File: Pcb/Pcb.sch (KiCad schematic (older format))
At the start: 129 parts, among them J1 TRRS, Q1 2N7002, SW1 SW_Push, SW10 SW_Push, SW11 SW_Push, SW12 SW_Push, SW13 SW_Push, SW14 SW_Push, SW15 SW_Push, SW16 SW_Push, SW17 SW_Push, SW18 SW_Push, SW19 SW_Push, SW2 SW2, SW20 SW_Push, SW21 SW_Push, SW22 SW_Push, SW23 SW_Push, SW24 SW_Push, SW25 SW_Push, SW26 SW_Push, SW27 SW_Push, SW28 SW_Push, SW29 SW_Push, SW3 SW_Push, SW4 SW_Push, SW5 SW_Push, SW6 SW_Push, SW7 SW_Push, SW8 SW_Push, SW9 SW_Push, U1 ProMicro

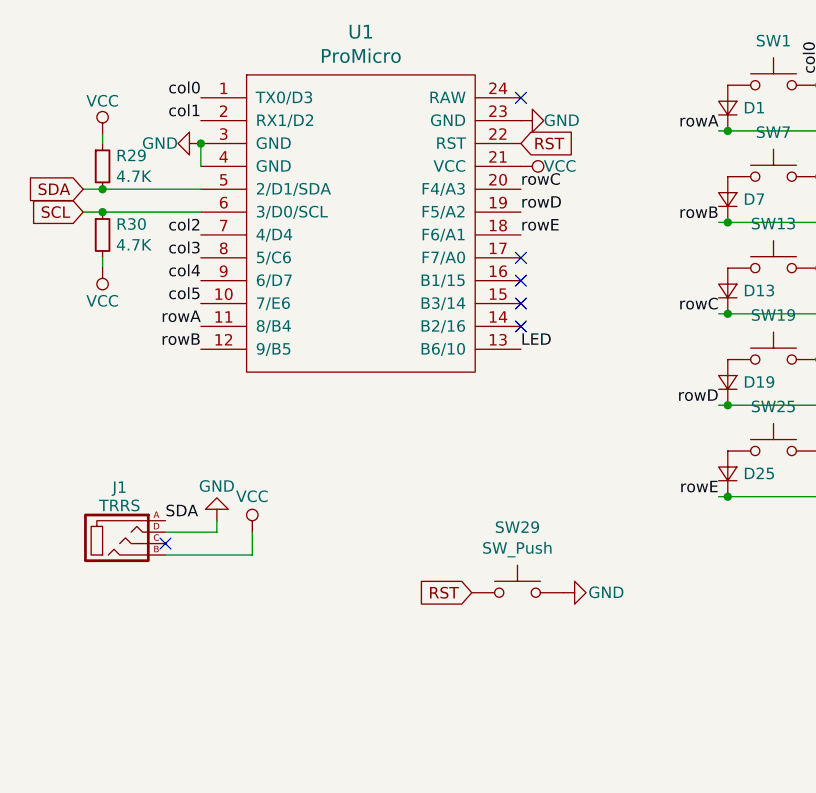
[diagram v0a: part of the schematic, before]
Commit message: Add jumpers for TRRS jack
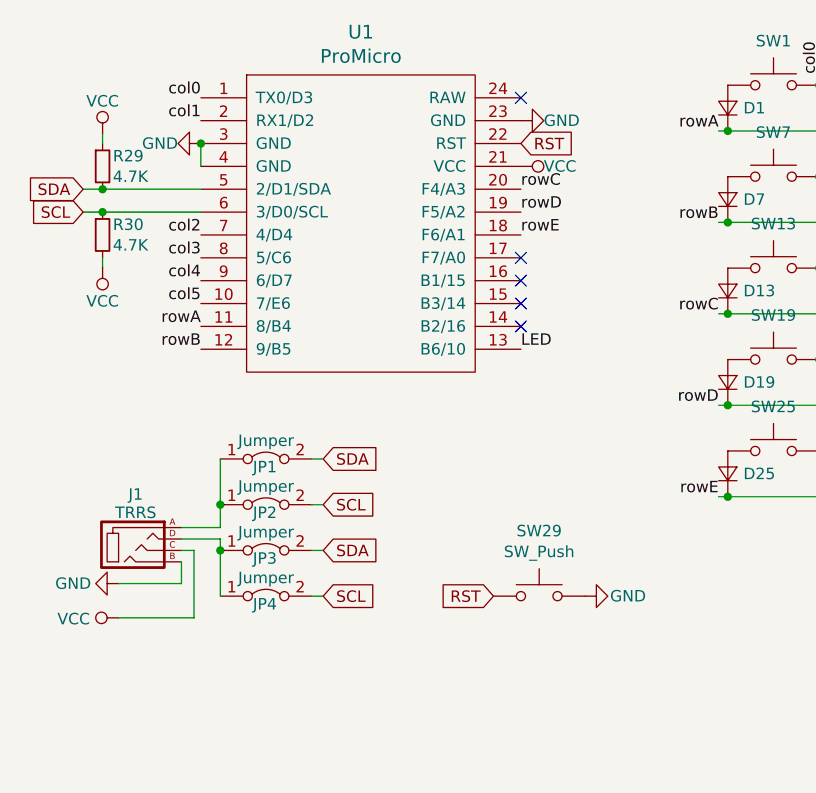
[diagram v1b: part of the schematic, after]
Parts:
- added JP1, JP2, JP3, JP4: Jumper, symbol Jumper:Jumper_2_Bridged
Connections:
- net GND: now also J1.B; no longer J1.D
- net SCL: now also JP2.2 (B), JP4.2 (B)
- net SDA: now also JP1.2 (B), JP3.2 (B); no longer J1.A
- net VCC: now also J1.C; no longer J1.B
- new net: J1.A, JP1.1 (A), JP2.1 (A)
- new net: J1.D, JP3.1 (A), JP4.1 (A)
- no-connect marks 6 -> 5
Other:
- moved on the sheet: J1, SW29
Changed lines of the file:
@@
 L Switch:SW_Push SW29
 U 1 1 5DBF73FF
-P 2625 3110
-F 0 "SW29" H 2625 3395 50  0000 C CNN
-F 1 "SW_Push" H 2625 3304 50  0000 C CNN
-F 2 "Used_Footprints:Switch_Reset_THT" H 2625 3310 50  0001 C CNN
-F 3 "~" H 2625 3310 50  0001 C CNN
-	1    2625 3110
+P 2720 3125
+F 0 "SW29" H 2720 3410 50  0000 C CNN
+F 1 "SW_Push" H 2720 3319 50  0000 C CNN
+F 2 "Used_Footprints:Switch_Reset_THT" H 2720 3325 50  0001 C CNN
+F 3 "~" H 2720 3325 50  0001 C CNN
+	1    2720 3125
 	1    0    0    -1
 $EndComp
@@
 L power:GND #PWR01
 U 1 1 5DBF973E
-P 2825 3110
-F 0 "#PWR01" H 2825 2860 50  0001 C CNN
-F 1 "GND" V 2825 3000 50  0000 R CNN
-F 2 "" H 2825 3110 50  0001 C CNN
-F 3 "" H 2825 3110 50  0001 C CNN
-	1    2825 3110
+P 2920 3125
+F 0 "#PWR01" H 2920 2875 50  0001 C CNN
+F 1 "GND" V 2920 3015 50  0000 R CNN
+F 2 "" H 2920 3125 50  0001 C CNN
+F 3 "" H 2920 3125 50  0001 C CNN
+	1    2920 3125
 	0    -1   -1   0
 $EndComp
@@
 L kbd:MJ-4PP-9 J1
 U 1 1 5DBFACF7
-P 885 2870
-F 0 "J1" H 885 3090 50  0000 C CNN
-F 1 "TRRS" H 885 3010 50  0000 C CNN
-F 2 "Used_Footprints:TRSS_DUAL_THT" H 1160 3045 50  0001 C CNN
-F 3 "~" H 1160 3045 50  0001 C CNN
-	1    885  2870
-	1    0    0    -1
-$EndComp
-Text GLabel 2425 3110 0    50   Input ~ 0
+P 955 2900
+F 0 "J1" H 955 3120 50  0000 C CNN
+F 1 "TRRS" H 955 3040 50  0000 C CNN
+F 2 "Used_Footprints:TRSS_DUAL_THT" H 1230 3075 50  0001 C CNN
+F 3 "~" H 1230 3075 50  0001 C CNN
+	1    955  2900
+	1    0    0    -1
+$EndComp
+Text GLabel 2520 3125 0    50   Input ~ 0
 RST
 Text GLabel 2640 1145 2    50   Input ~ 0
@@
 NoConn ~ 2640 1845
 NoConn ~ 2640 1745
-Text Label 1085 2795 0    50   ~ 0
-SDA
-$Comp
-L power:GND #PWR0101
-U 1 1 5E5516DF
-P 1310 2795
-F 0 "#PWR0101" H 1310 2545 50  0001 C CNN
-F 1 "GND" H 1310 2645 50  0000 C CNN
-F 2 "" H 1310 2795 50  0001 C CNN
-F 3 "" H 1310 2795 50  0001 C CNN
-	1    1310 2795
-	-1   0    0    1
-$EndComp
-Wire Wire Line
-	1085 2845 1310 2845
-Wire Wire Line
-	1310 2845 1310 2795
-$Comp
-L power:VCC #PWR0102
-U 1 1 5E557C13
-P 1465 2845
-F 0 "#PWR0102" H 1465 2695 50  0001 C CNN
-F 1 "VCC" H 1465 3000 50  0000 C CNN
-F 2 "" H 1465 2845 50  0001 C CNN
-F 3 "" H 1465 2845 50  0001 C CNN
-	1    1465 2845
-	1    0    0    -1
-$EndComp
-Wire Wire Line
-	1465 2845 1465 2945
-Wire Wire Line
-	1465 2945 1085 2945
-NoConn ~ 1085 2895
 Connection ~ 1240 1145
 $Comp
@@
 U 1 1 5E5A5774
 P 810 1245
-F 0 "R29" H 869 1291 50  0000 L CNN
-F 1 "4.7K" H 869 1200 50  0000 L CNN
+F 0 "R29" H 855 1290 50  0000 L CNN
+F 1 "4.7K" H 855 1200 50  0000 L CNN
 F 2 "" H 810 1245 50  0001 C CNN
 F 3 "~" H 810 1245 50  0001 C CNN
@@
 U 1 1 5E5A67AE
 P 810 1545
-F 0 "R30" H 869 1591 50  0000 L CNN
-F 1 "4.7K" H 869 1500 50  0000 L CNN
+F 0 "R30" H 855 1590 50  0000 L CNN
+F 1 "4.7K" H 855 1500 50  0000 L CNN
 F 2 "" H 810 1545 50  0001 C CNN
 F 3 "~" H 810 1545 50  0001 C CNN
@@
 Wire Wire Line
 	810  1105 810  1145
+$Comp
+L Jumper:Jumper_2_Bridged JP1
+U 1 1 5E612479
+P 1525 2525
+F 0 "JP1" H 1520 2490 50  0000 C CNN
+F 1 "Jumper" H 1525 2605 50  0000 C CNN
+F 2 "" H 1525 2525 50  0001 C CNN
+F 3 "~" H 1525 2525 50  0001 C CNN
+	1    1525 2525
+	1    0    0    -1
+$EndComp
+$Comp
+L Jumper:Jumper_2_Bridged JP2
+U 1 1 5E61A832
+P 1525 2725
+F 0 "JP2" H 1520 2690 50  0000 C CNN
+F 1 "Jumper" H 1525 2805 50  0000 C CNN
+F 2 "" H 1525 2725 50  0001 C CNN
+F 3 "~" H 1525 2725 50  0001 C CNN
+	1    1525 2725
+	1    0    0    -1
+$EndComp
+$Comp
+L Jumper:Jumper_2_Bridged JP3
+U 1 1 5E622F25
+P 1525 2925
+F 0 "JP3" H 1520 2890 50  0000 C CNN
+F 1 "Jumper" H 1525 3005 50  0000 C CNN
+F 2 "" H 1525 2925 50  0001 C CNN
+F 3 "~" H 1525 2925 50  0001 C CNN
+	1    1525 2925
+	1    0    0    -1
+$EndComp
+$Comp
+L Jumper:Jumper_2_Bridged JP4
+U 1 1 5E622F2B
+P 1525 3125
+F 0 "JP4" H 1520 3090 50  0000 C CNN
+F 1 "Jumper" H 1525 3205 50  0000 C CNN
+F 2 "" H 1525 3125 50  0001 C CNN
+F 3 "~" H 1525 3125 50  0001 C CNN
+	1    1525 3125
+	1    0    0    -1
+$EndComp
+Wire Wire Line
+	1325 2525 1325 2725
+Wire Wire Line
+	1325 2825 1155 2825
+Connection ~ 1325 2725
+Wire Wire Line
+	1325 2725 1325 2825
+Wire Wire Line
+	1325 3125 1325 2925
+Wire Wire Line
+	1325 2875 1155 2875
+Connection ~ 1325 2925
+Wire Wire Line
+	1325 2925 1325 2875
+Text GLabel 1775 2525 2    50   Input ~ 0
+SDA
+Wire Wire Line
+	1775 2525 1725 2525
+Text GLabel 1775 2725 2    50   Input ~ 0
+SCL
+Wire Wire Line
+	1775 2725 1725 2725
+Text GLabel 1775 2925 2    50   Input ~ 0
+SDA
+Wire Wire Line
+	1775 2925 1725 2925
+Text GLabel 1775 3125 2    50   Input ~ 0
+SCL
+Wire Wire Line
+	1775 3125 1725 3125
+$Comp
+L power:GND #PWR?
+U 1 1 5E653D30
+P 880 3070
+F 0 "#PWR?" H 880 2820 50  0001 C CNN
+F 1 "GND" V 880 2950 50  0000 R CNN
+F 2 "" H 880 3070 50  0001 C CNN
+F 3 "" H 880 3070 50  0001 C CNN
+	1    880  3070
+	0    1    1    0
+$EndComp
+Wire Wire Line
+	880  3070 1155 3070
+Wire Wire Line
+	1155 3070 1155 2975
+$Comp
+L power:VCC #PWR?
+U 1 1 5E65ED2C
+P 880 3220
+F 0 "#PWR?" H 880 3070 50  0001 C CNN
+F 1 "VCC" V 875 3345 50  0000 L CNN
+F 2 "" H 880 3220 50  0001 C CNN
+F 3 "" H 880 3220 50  0001 C CNN
+	1    880  3220
+	0    -1   -1   0
+$EndComp
+Wire Wire Line
+	1210 3220 1210 2925
+Wire Wire Line
+	1210 2925 1155 2925
+Wire Wire Line
+	880  3220 1210 3220
 $EndSCHEMATC

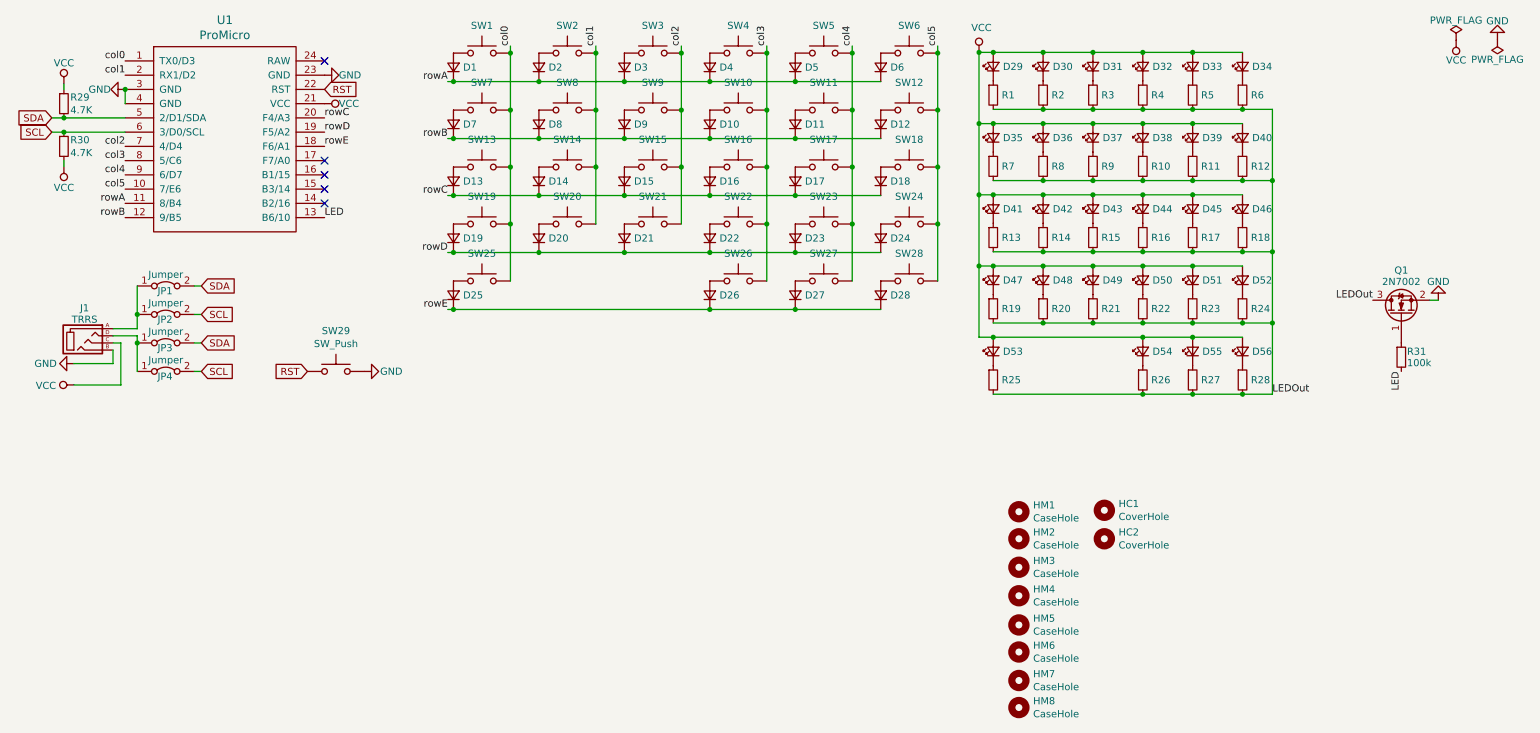
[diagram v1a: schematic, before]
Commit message: Add value for resistors
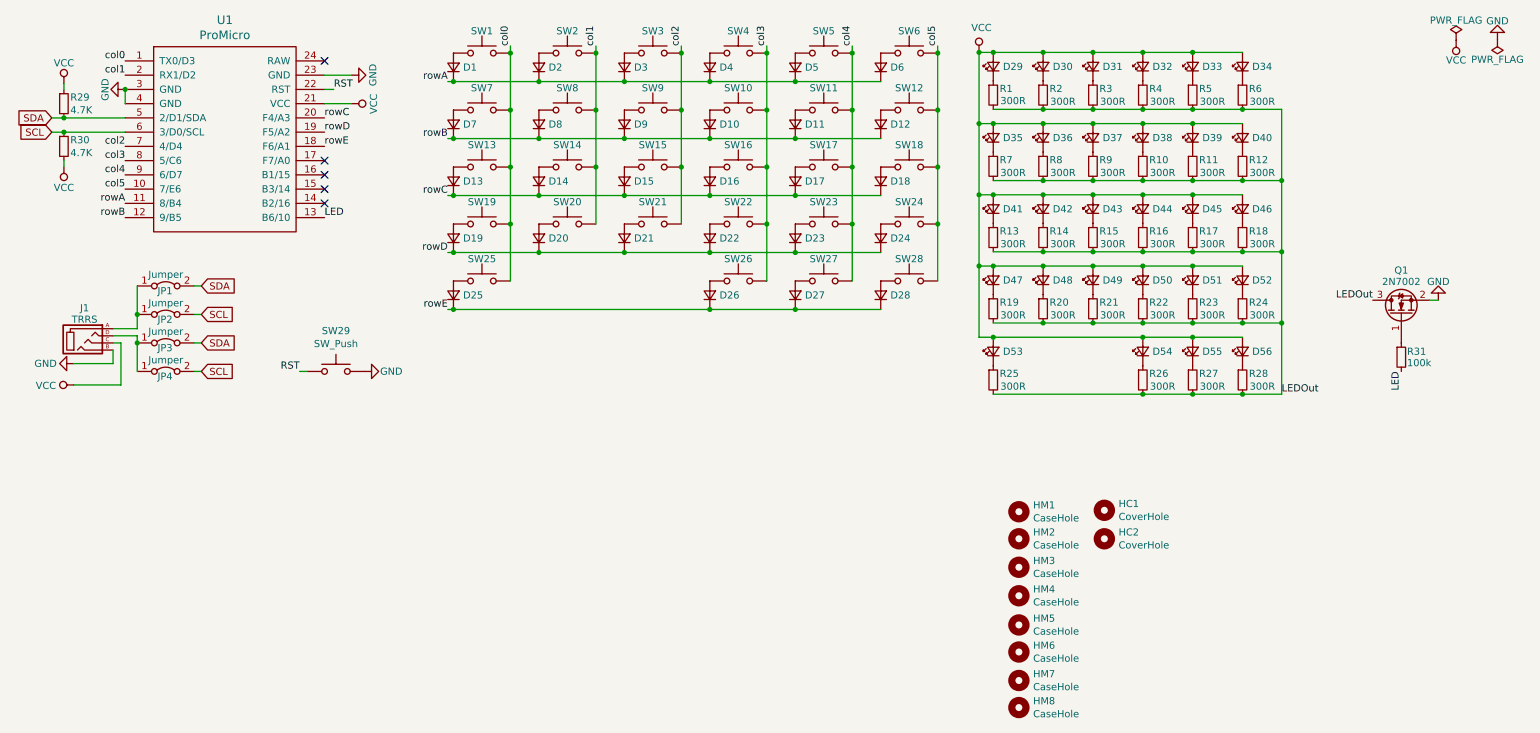
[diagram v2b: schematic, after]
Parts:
- R1, R10, R11, R12, R13, R14, R15, R16, R17, R18, R19, R2, R20, R21, R22, R23, R24, R25, R26, R27, R28, R3, R4, R5, R6, R7, R8, R9: value R_Small -> 300R

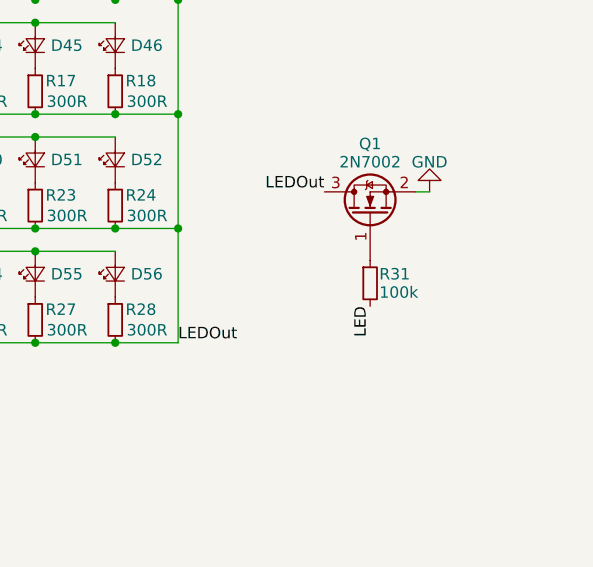
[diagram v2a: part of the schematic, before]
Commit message: Add value for diodes
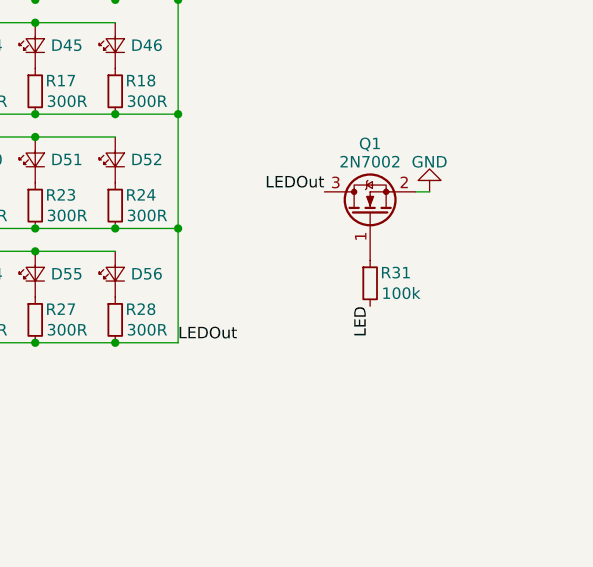
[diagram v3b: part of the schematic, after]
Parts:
- D1, D10, D11, D12, D13, D14, D15, D16, D17, D18, D19, D2, D20, D21, D22, D23, D24, D25, D26, D27, D28, D3, D4, D5, D6, D7, D8, D9: value D_Small -> 1N4148
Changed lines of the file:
@@
 P 3545 990
 F 0 "D1" V 3545 922 50  0000 R CNN
-F 1 "D_Small" V 3500 922 50  0001 R CNN
+F 1 "1N4148" V 3500 922 50  0001 R CNN
 F 2 "Used_Footprints:Diode_Hybrid_SOD-123" V 3545 990 50  0001 C CNN
 F 3 "~" V 3545 990 50  0001 C CNN
@@
 P 4145 990
 F 0 "D2" V 4145 922 50  0000 R CNN
-F 1 "D_Small" V 4100 922 50  0001 R CNN
+F 1 "1N4148" V 4100 922 50  0001 R CNN
 F 2 "Used_Footprints:Diode_Hybrid_SOD-123" V 4145 990 50  0001 C CNN
 F 3 "~" V 4145 990 50  0001 C CNN
@@
 P 4745 990
 F 0 "D3" V 4745 922 50  0000 R CNN
-F 1 "D_Small" V 4700 922 50  0001 R CNN
+F 1 "1N4148" V 4700 922 50  0001 R CNN
 F 2 "Used_Footprints:Diode_Hybrid_SOD-123" V 4745 990 50  0001 C CNN
 F 3 "~" V 4745 990 50  0001 C CNN
@@
 P 5345 990
 F 0 "D4" V 5345 922 50  0000 R CNN
-F 1 "D_Small" V 5300 922 50  0001 R CNN
+F 1 "1N4148" V 5300 922 50  0001 R CNN
 F 2 "Used_Footprints:Diode_Hybrid_SOD-123" V 5345 990 50  0001 C CNN
 F 3 "~" V 5345 990 50  0001 C CNN
@@
 P 5945 990
 F 0 "D5" V 5945 922 50  0000 R CNN
-F 1 "D_Small" V 5900 922 50  0001 R CNN
+F 1 "1N4148" V 5900 922 50  0001 R CNN
 F 2 "Used_Footprints:Diode_Hybrid_SOD-123" V 5945 990 50  0001 C CNN
 F 3 "~" V 5945 990 50  0001 C CNN
@@
 P 6545 990
 F 0 "D6" V 6545 922 50  0000 R CNN
-F 1 "D_Small" V 6500 922 50  0001 R CNN
+F 1 "1N4148" V 6500 922 50  0001 R CNN
 F 2 "Used_Footprints:Diode_Hybrid_SOD-123" V 6545 990 50  0001 C CNN
 F 3 "~" V 6545 990 50  0001 C CNN
@@
 P 3545 1390
 F 0 "D7" V 3545 1322 50  0000 R CNN
-F 1 "D_Small" V 3500 1322 50  0001 R CNN
+F 1 "1N4148" V 3500 1322 50  0001 R CNN
 F 2 "Used_Footprints:Diode_Hybrid_SOD-123" V 3545 1390 50  0001 C CNN
 F 3 "~" V 3545 1390 50  0001 C CNN
@@
 P 4145 1390
 F 0 "D8" V 4145 1322 50  0000 R CNN
-F 1 "D_Small" V 4100 1322 50  0001 R CNN
+F 1 "1N4148" V 4100 1322 50  0001 R CNN
 F 2 "Used_Footprints:Diode_Hybrid_SOD-123" V 4145 1390 50  0001 C CNN
 F 3 "~" V 4145 1390 50  0001 C CNN
@@
 P 4745 1390
 F 0 "D9" V 4745 1322 50  0000 R CNN
-F 1 "D_Small" V 4700 1322 50  0001 R CNN
+F 1 "1N4148" V 4700 1322 50  0001 R CNN
 F 2 "Used_Footprints:Diode_Hybrid_SOD-123" V 4745 1390 50  0001 C CNN
 F 3 "~" V 4745 1390 50  0001 C CNN
@@
 P 5345 1390
 F 0 "D10" V 5345 1322 50  0000 R CNN
-F 1 "D_Small" V 5300 1322 50  0001 R CNN
+F 1 "1N4148" V 5300 1322 50  0001 R CNN
 F 2 "Used_Footprints:Diode_Hybrid_SOD-123" V 5345 1390 50  0001 C CNN
 F 3 "~" V 5345 1390 50  0001 C CNN
@@
 P 5945 1390
 F 0 "D11" V 5945 1322 50  0000 R CNN
-F 1 "D_Small" V 5900 1322 50  0001 R CNN
+F 1 "1N4148" V 5900 1322 50  0001 R CNN
 F 2 "Used_Footprints:Diode_Hybrid_SOD-123" V 5945 1390 50  0001 C CNN
 F 3 "~" V 5945 1390 50  0001 C CNN
@@
 P 6545 1390
 F 0 "D12" V 6545 1322 50  0000 R CNN
-F 1 "D_Small" V 6500 1322 50  0001 R CNN
+F 1 "1N4148" V 6500 1322 50  0001 R CNN
 F 2 "Used_Footprints:Diode_Hybrid_SOD-123" V 6545 1390 50  0001 C CNN
 F 3 "~" V 6545 1390 50  0001 C CNN
@@
 P 3545 1790
 F 0 "D13" V 3545 1722 50  0000 R CNN
-F 1 "D_Small" V 3500 1722 50  0001 R CNN
+F 1 "1N4148" V 3500 1722 50  0001 R CNN
 F 2 "Used_Footprints:Diode_Hybrid_SOD-123" V 3545 1790 50  0001 C CNN
 F 3 "~" V 3545 1790 50  0001 C CNN
@@
 P 4145 1790
 F 0 "D14" V 4145 1722 50  0000 R CNN
-F 1 "D_Small" V 4100 1722 50  0001 R CNN
+F 1 "1N4148" V 4100 1722 50  0001 R CNN
 F 2 "Used_Footprints:Diode_Hybrid_SOD-123" V 4145 1790 50  0001 C CNN
 F 3 "~" V 4145 1790 50  0001 C CNN
@@
 P 4745 1790
 F 0 "D15" V 4745 1722 50  0000 R CNN
-F 1 "D_Small" V 4700 1722 50  0001 R CNN
+F 1 "1N4148" V 4700 1722 50  0001 R CNN
 F 2 "Used_Footprints:Diode_Hybrid_SOD-123" V 4745 1790 50  0001 C CNN
 F 3 "~" V 4745 1790 50  0001 C CNN
@@
 P 5345 1790
 F 0 "D16" V 5345 1722 50  0000 R CNN
-F 1 "D_Small" V 5300 1722 50  0001 R CNN
+F 1 "1N4148" V 5300 1722 50  0001 R CNN
 F 2 "Used_Footprints:Diode_Hybrid_SOD-123" V 5345 1790 50  0001 C CNN
 F 3 "~" V 5345 1790 50  0001 C CNN
@@
 P 5945 1790
 F 0 "D17" V 5945 1722 50  0000 R CNN
-F 1 "D_Small" V 5900 1722 50  0001 R CNN
+F 1 "1N4148" V 5900 1722 50  0001 R CNN
 F 2 "Used_Footprints:Diode_Hybrid_SOD-123" V 5945 1790 50  0001 C CNN
 F 3 "~" V 5945 1790 50  0001 C CNN
@@
 P 6545 1790
 F 0 "D18" V 6545 1722 50  0000 R CNN
-F 1 "D_Small" V 6500 1722 50  0001 R CNN
+F 1 "1N4148" V 6500 1722 50  0001 R CNN
 F 2 "Used_Footprints:Diode_Hybrid_SOD-123" V 6545 1790 50  0001 C CNN
 F 3 "~" V 6545 1790 50  0001 C CNN
@@
 P 3545 2190
 F 0 "D19" V 3545 2122 50  0000 R CNN
-F 1 "D_Small" V 3500 2122 50  0001 R CNN
+F 1 "1N4148" V 3500 2122 50  0001 R CNN
 F 2 "Used_Footprints:Diode_Hybrid_SOD-123" V 3545 2190 50  0001 C CNN
 F 3 "~" V 3545 2190 50  0001 C CNN
@@
 P 4145 2190
 F 0 "D20" V 4145 2122 50  0000 R CNN
-F 1 "D_Small" V 4100 2122 50  0001 R CNN
+F 1 "1N4148" V 4100 2122 50  0001 R CNN
 F 2 "Used_Footprints:Diode_Hybrid_SOD-123" V 4145 2190 50  0001 C CNN
 F 3 "~" V 4145 2190 50  0001 C CNN
@@
 P 4745 2190
 F 0 "D21" V 4745 2122 50  0000 R CNN
-F 1 "D_Small" V 4700 2122 50  0001 R CNN
+F 1 "1N4148" V 4700 2122 50  0001 R CNN
 F 2 "Used_Footprints:Diode_Hybrid_SOD-123" V 4745 2190 50  0001 C CNN
 F 3 "~" V 4745 2190 50  0001 C CNN
@@
 P 5345 2190
 F 0 "D22" V 5345 2122 50  0000 R CNN
-F 1 "D_Small" V 5300 2122 50  0001 R CNN
+F 1 "1N4148" V 5300 2122 50  0001 R CNN
 F 2 "Used_Footprints:Diode_Hybrid_SOD-123" V 5345 2190 50  0001 C CNN
 F 3 "~" V 5345 2190 50  0001 C CNN
@@
 P 5945 2190
 F 0 "D23" V 5945 2122 50  0000 R CNN
-F 1 "D_Small" V 5900 2122 50  0001 R CNN
+F 1 "1N4148" V 5900 2122 50  0001 R CNN
 F 2 "Used_Footprints:Diode_Hybrid_SOD-123" V 5945 2190 50  0001 C CNN
 F 3 "~" V 5945 2190 50  0001 C CNN
@@
 P 6545 2190
 F 0 "D24" V 6545 2122 50  0000 R CNN
-F 1 "D_Small" V 6500 2122 50  0001 R CNN
+F 1 "1N4148" V 6500 2122 50  0001 R CNN
 F 2 "Used_Footprints:Diode_Hybrid_SOD-123" V 6545 2190 50  0001 C CNN
 F 3 "~" V 6545 2190 50  0001 C CNN
@@
 P 3545 2590
 F 0 "D25" V 3545 2522 50  0000 R CNN
-F 1 "D_Small" V 3500 2522 50  0001 R CNN
+F 1 "1N4148" V 3500 2522 50  0001 R CNN
 F 2 "Used_Footprints:Diode_Hybrid_SOD-123" V 3545 2590 50  0001 C CNN
 F 3 "~" V 3545 2590 50  0001 C CNN
@@
 P 5345 2590
 F 0 "D26" V 5345 2522 50  0000 R CNN
-F 1 "D_Small" V 5300 2522 50  0001 R CNN
+F 1 "1N4148" V 5300 2522 50  0001 R CNN
 F 2 "Used_Footprints:Diode_Hybrid_SOD-123" V 5345 2590 50  0001 C CNN
 F 3 "~" V 5345 2590 50  0001 C CNN
@@
 P 5945 2590
 F 0 "D27" V 5945 2522 50  0000 R CNN
-F 1 "D_Small" V 5900 2522 50  0001 R CNN
+F 1 "1N4148" V 5900 2522 50  0001 R CNN
 F 2 "Used_Footprints:Diode_Hybrid_SOD-123" V 5945 2590 50  0001 C CNN
 F 3 "~" V 5945 2590 50  0001 C CNN
@@
 P 6545 2590
 F 0 "D28" V 6545 2522 50  0000 R CNN
-F 1 "D_Small" V 6500 2522 50  0001 R CNN
+F 1 "1N4148" V 6500 2522 50  0001 R CNN
 F 2 "Used_Footprints:Diode_Hybrid_SOD-123" V 6545 2590 50  0001 C CNN
 F 3 "~" V 6545 2590 50  0001 C CNN
@@
 U 1 1 5DB7D24B
 P 10200 3025
-F 0 "R31" H 10240 3065 50  0000 L CNN
-F 1 "100k" H 10240 2985 50  0000 L CNN
+F 0 "R31" H 10245 3070 50  0000 L CNN
+F 1 "100k" H 10250 2980 50  0000 L CNN
 F 2 "Used_Footprints:Resistor_Hybrid_1205" H 10200 3025 50  0001 C CNN
 F 3 "~" H 10200 3025 50  0001 C CNN
